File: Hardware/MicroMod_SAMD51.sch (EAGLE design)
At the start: 30 parts, among them J2 MICROMOD-2222, U1 W25QXX128MBIT-6X5-NO_CENTER, U2 ATSAMD51J20A-A, Y1 32.768kHz

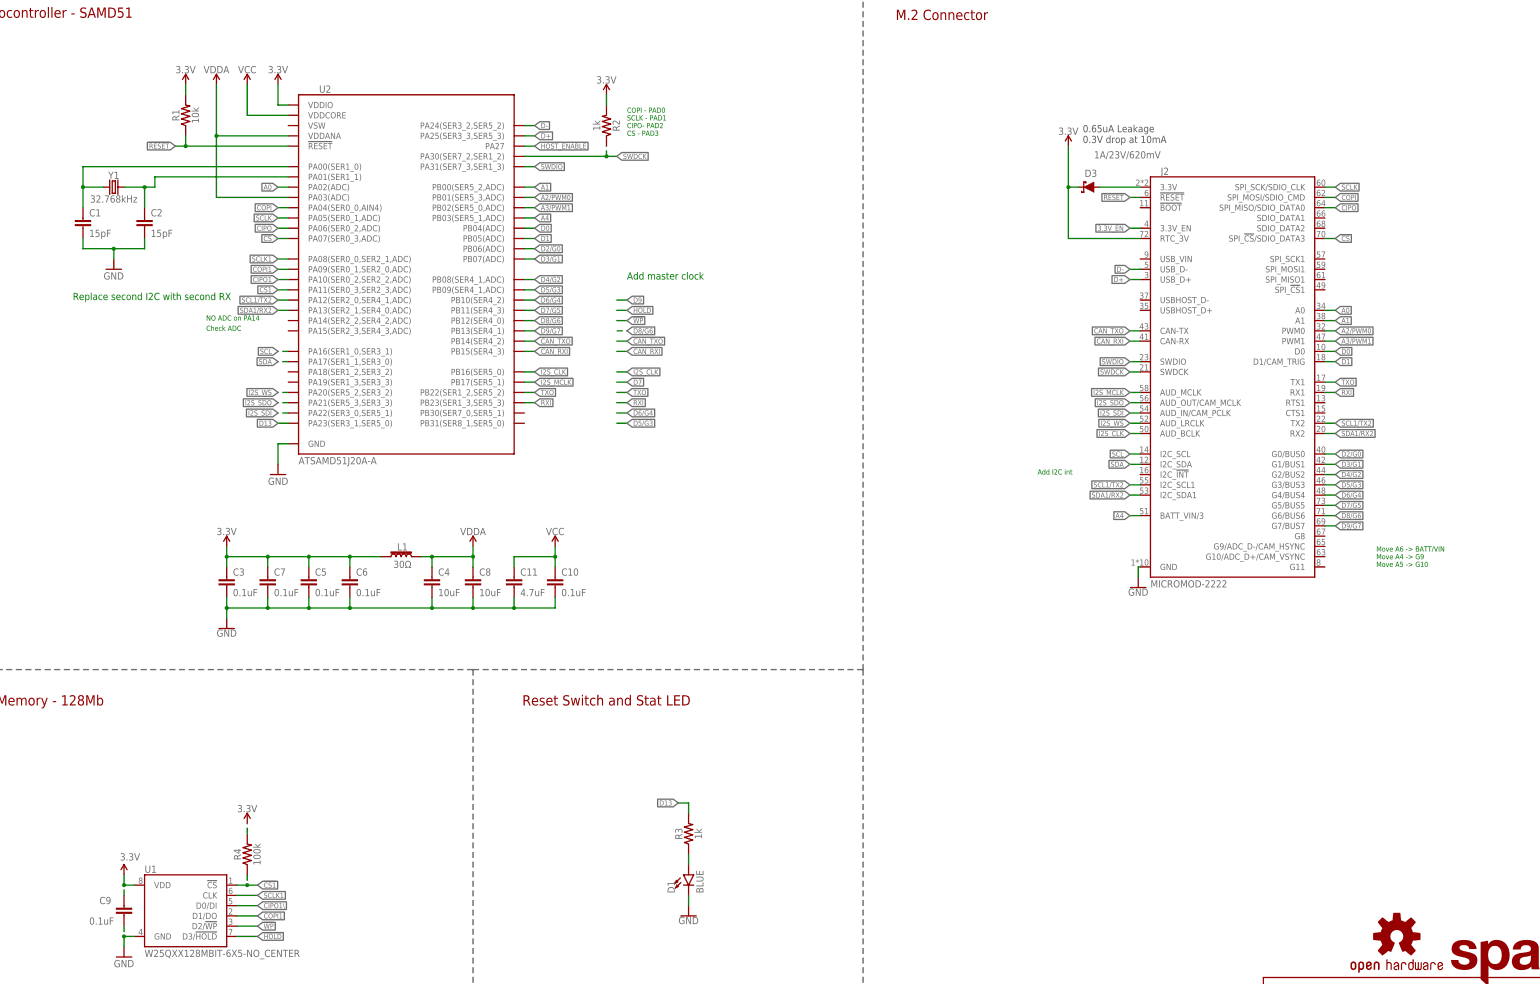
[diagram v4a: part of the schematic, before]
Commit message: Begins routing, removes old
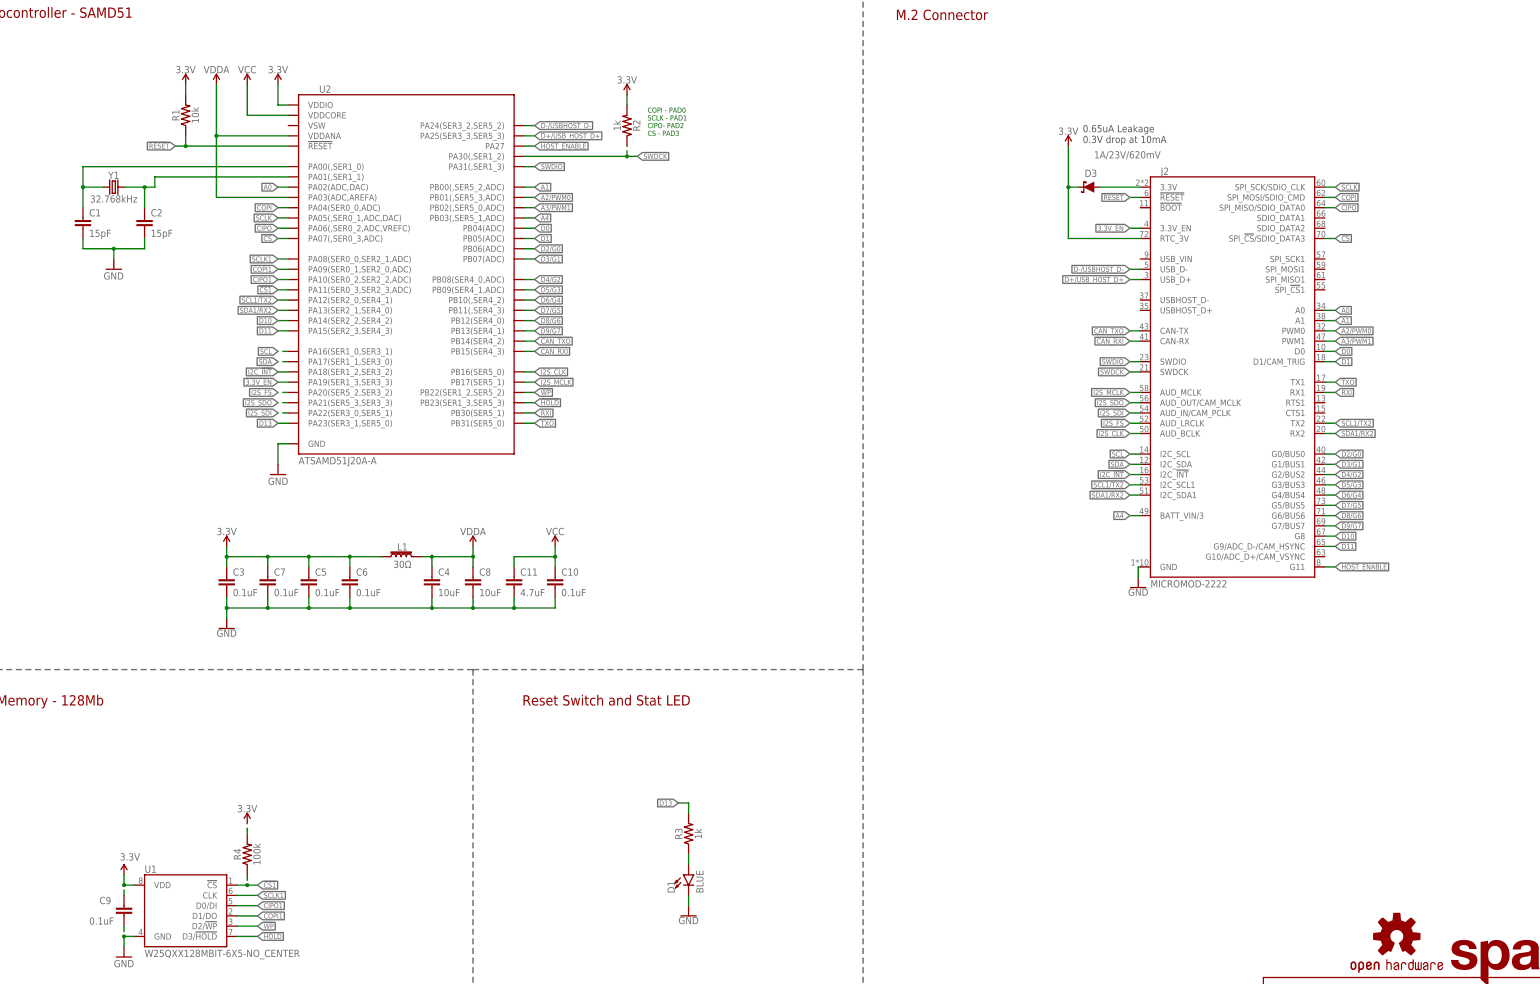
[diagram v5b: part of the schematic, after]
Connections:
- net D+ renamed D+/USB_HOST_D+
- net D- renamed D-/USBHOST_D-
- net I2S_WS renamed I2S_FS
- removed net CIPO1\: U1.D0/DI
- removed net CS1: U2.PA11(SER0_3,SER2_3,ADC)
- new net D10: J2.G8, U2.PA14(SER2_2,SER4_2)
- new net D11: J2.G9/ADC_D-/CAM_HSYNC, U2.PA15(SER2_3,SER4_3)
- new net I2C_!INT!: J2.I2C_!INT!, U2.PA18(SER1_2,SER3_2)
- net !CS: now also U2.PA07(,SER0_3,ADC); no longer U2.PA07(SER0_3,ADC)
- net !CS1!: now also U2.PA11(SER0_3,SER2_3,ADC)
- net !HOLD!: now also U2.PB23(SER1_3,SER5_3)
- net !WP!: now also U2.PB22(SER1_2,SER5_2)
- net 3.3V_EN: now also U2.PA19(SER1_3,SER3_3)
- net A0: now also U2.PA02(ADC,DAC); no longer U2.PA02(ADC)
- net A1: now also U2.PB00(,SER5_2,ADC); no longer U2.PB00(SER5_2,ADC)
- net A2/PWM0: now also U2.PB01(,SER5_3,ADC); no longer U2.PB01(SER5_3,ADC)
- net A3/PWM1: now also U2.PB02(,SER5_0,ADC); no longer U2.PB02(SER5_0,ADC)
- net A4: now also U2.PB03(,SER5_1,ADC); no longer U2.PB03(SER5_1,ADC)
- net CIPO: now also U2.PA06(,SER0_2,ADC,VREFC); no longer U2.PA06(SER0_2,ADC)
- net CIPO1: now also U1.D0/DI
- net COPI: now also U2.PA04(SER0_0,ADC); no longer U2.PA04(SER0_0,AIN4)
- net D4/G2: now also U2.PB08(SER4_0,ADC); no longer U2.PB08(SER4_1,ADC)
- net D6/G4: now also U2.PB10(,SER4_2); no longer U2.PB10(SER4_2)
- net D7/G5: now also U2.PB11(,SER4_3); no longer U2.PB11(SER4_3)
- net HOST_ENABLE: now also J2.G11
- net RXI: now also U2.PB30(SER5_1); no longer U2.PB23(SER1_3,SER5_3)
- net SCL1/TX2: now also U2.PA12(SER2_0,SER4_1); no longer U2.PA12(SER2_0,SER4_1,ADC)
- net SCLK: now also U2.PA05(,SER0_1,ADC,DAC); no longer U2.PA05(SER0_1,ADC)
- net SDA1/RX2: now also U2.PA13(SER2_1,SER4_0); no longer U2.PA13(SER2_1,SER4_0,ADC)
- net SWDCK: now also U2.PA30(,SER1_2); no longer U2.PA30(SER7_2,SER1_2)
- net SWDIO: now also U2.PA31(,SER1_3); no longer U2.PA31(SER7_3,SER1_3)
- net TXO: now also U2.PB31(SER5_0); no longer U2.PB22(SER1_2,SER5_2)
- net VDDA: now also U2.PA03(ADC,AREFA); no longer U2.PA03(ADC)
- net XIN32: now also U2.PA00(,SER1_0); no longer U2.PA00(SER1_0)
- net XOUT32: now also U2.PA01(,SER1_1); no longer U2.PA01(SER1_1)
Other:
- note removed: "Add I2C int"
- note removed: "Add master clock"
- note removed: "Check ADC"
- note removed: "Move A6 -> BATT/VIN Move A4 -> G9 Move A5 -> G10"
- note removed: "NO ADC on PA14"
- note removed: "Replace second I2C with second RX"
- moved on the sheet: R2

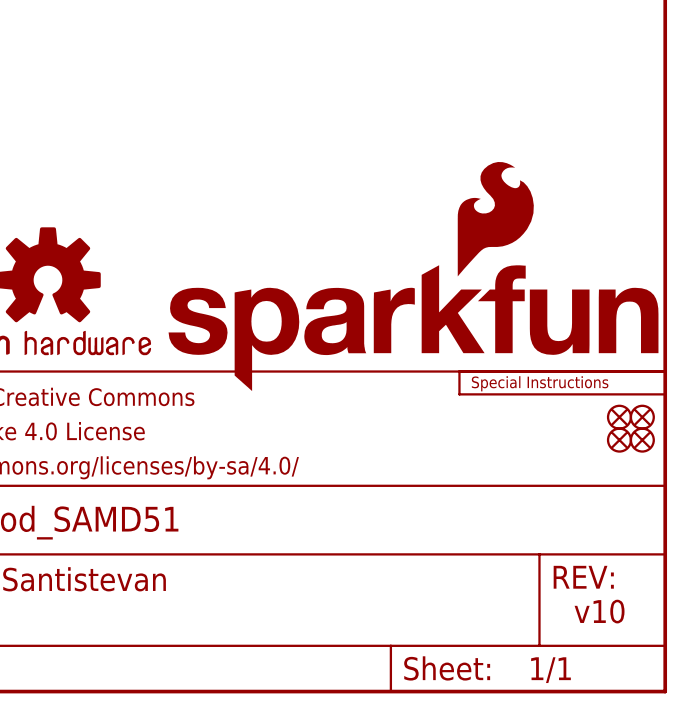
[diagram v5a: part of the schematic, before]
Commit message: Updates SparkFun silk, rolls version to v11, fixes some traces that were not crossing others at 90 degrees.
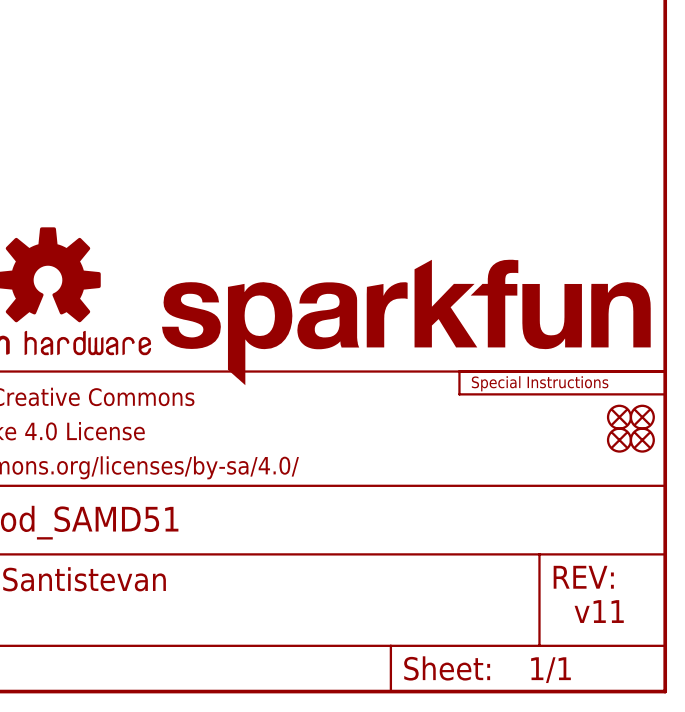
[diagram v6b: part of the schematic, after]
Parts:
- LOGO6: value SFE_LOGO_NAME_FLAME.1_INCH -> SFE_LOGO_NAME.1_INCH; device SparkFun-Aesthetics:SFE_LOGO_NAME_FLAME.1_INCH -> SparkFun-Aesthetics:SFE_LOGO_NAME.1_INCH
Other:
- note added: "v11"
- note removed: "v10"
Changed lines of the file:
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@@
 <part name="LOGO2" library="SparkFun-Aesthetics" deviceset="OSHW-LOGO" device="MINI" value="OSHW-LOGOMINI"/>
 <part name="LOGO5" library="SparkFun-Aesthetics" deviceset="SPECIAL_INSTRUCTIONS" device="-ORDERING"/>
-<part name="LOGO6" library="SparkFun-Aesthetics" deviceset="SFE_LOGO_NAME_FLAME" device=".1_INCH"/>
+<part name="LOGO6" library="SparkFun-Aesthetics" deviceset="SFE_LOGO_NAME" device=".1_INCH"/>
 <part name="FRAME2" library="SparkFun-Aesthetics" deviceset="FRAME-LEDGER" device=""/>
 <part name="D1" library="SparkFun-LED" deviceset="LED-BLUE" device="0603" value="BLUE"/>
@@
 <sheet>
 <plain>
-<text x="421.64" y="7.62" size="2.54" layer="94" font="vector">v10</text>
+<text x="421.64" y="7.62" size="2.54" layer="94" font="vector">v11</text>
 <text x="250.64" y="273.78" size="2.54" layer="94" font="vector" align="center">M.2 Connector</text>
 <wire x1="231.14" y1="279.4" x2="231.14" y2="111.76" width="0.1524" layer="97" style="longdash"/>
@@
 <instance part="LOGO2" gate="G$1" x="363.22" y="45.72" smashed="yes"/>
 <instance part="LOGO5" gate="G$1" x="408.94" y="33.02" smashed="yes"/>
-<instance part="LOGO6" gate="G$1" x="375.92" y="33.02" smashed="yes"/>
+<instance part="LOGO6" gate="G$1" x="373.888" y="34.036" smashed="yes"/>
 <instance part="FRAME2" gate="G$1" x="0" y="0" smashed="yes"/>
 <instance part="FRAME2" gate="G$2" x="330.2" y="0" smashed="yes">

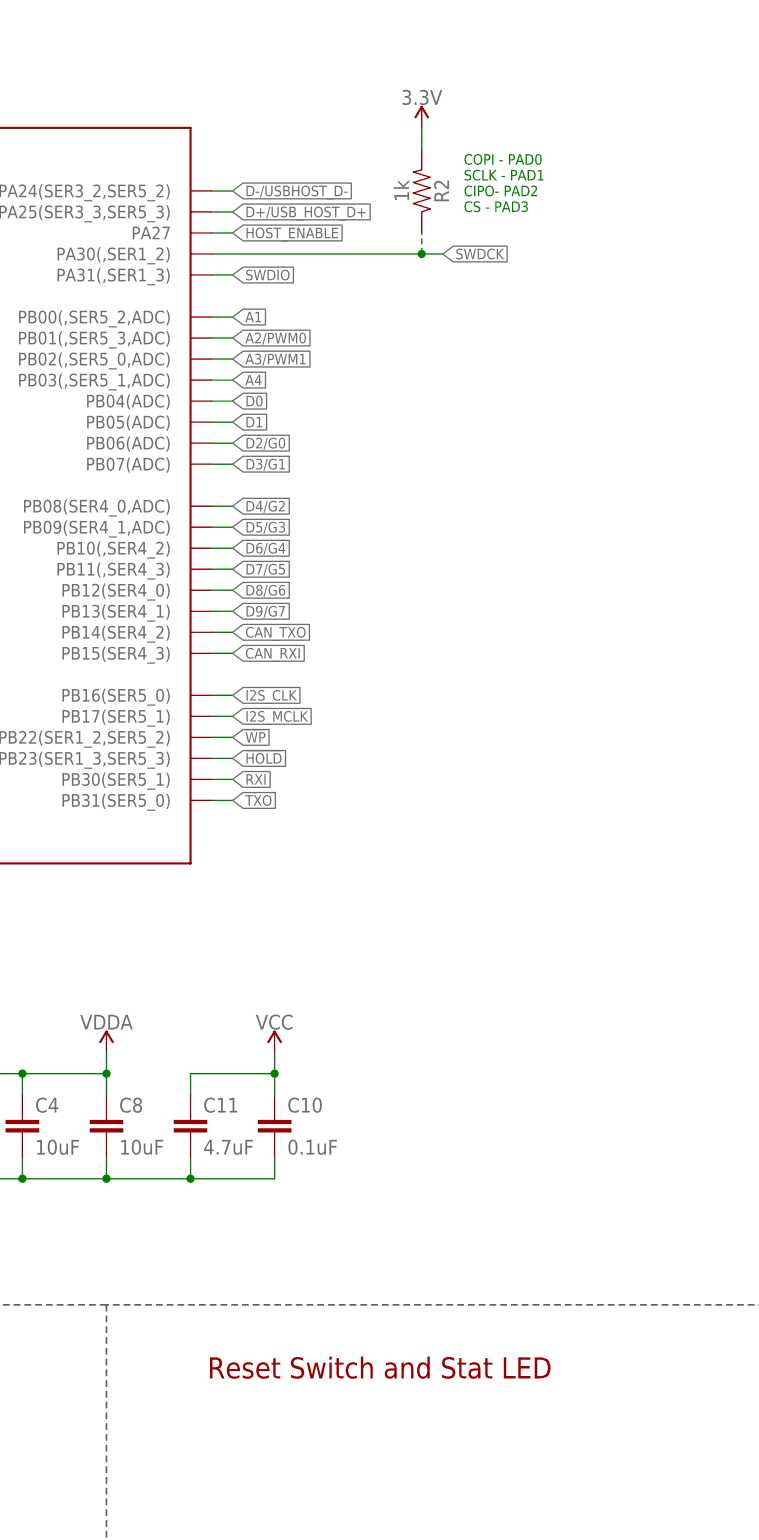
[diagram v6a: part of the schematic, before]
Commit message: Moves cap at top of board, adjusts USB differential pair
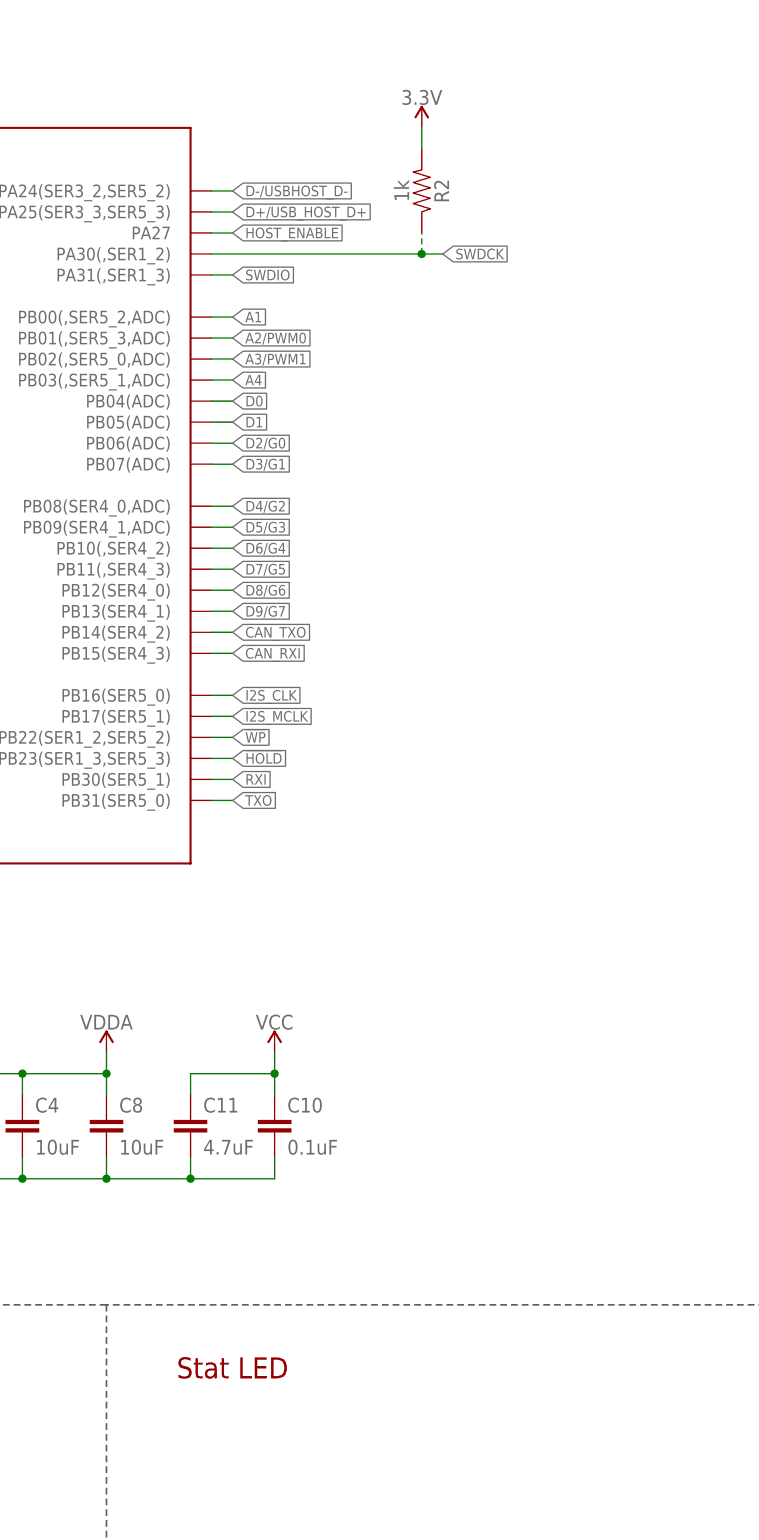
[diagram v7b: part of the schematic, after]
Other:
- note added: "Stat LED"
- note removed: "COPI - PAD0 SCLK - PAD1 CIPO- PAD2 CS - PAD3"
- note removed: "Reset Switch and Stat LED"
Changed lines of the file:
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@@
 <clearance class="1" value="0.2032"/>
+</class>
+<class number="2" name="USB" width="0.1016" drill="0">
+<clearance class="2" value="0.0762"/>
 </class>
 </classes>
@@
 <text x="30.48" y="274.32" size="2.54" layer="94" font="vector" align="center">Microcontroller - SAMD51</text>
 <text x="25.4" y="104.14" size="2.54" layer="94" font="vector" align="center">Flash Memory - 128Mb</text>
-<text x="167.64" y="104.14" size="2.54" layer="94" font="vector" align="center">Reset Switch and Stat LED</text>
+<text x="149.86" y="104.14" size="2.54" layer="94" font="vector" align="center">Stat LED</text>
 <wire x1="231.14" y1="111.76" x2="231.14" y2="0" width="0.2032" layer="97" style="longdash"/>
 <text x="349.758" y="11.176" size="2.54" layer="94" font="vector">Elias Santistevan</text>
 <text x="285.496" y="242.062" size="1.778" layer="97">0.65uA Leakage
 0.3V drop at 10mA</text>
-<text x="177.8" y="243.84" size="1.27" layer="91">COPI - PAD0
-SCLK - PAD1
-CIPO- PAD2
-CS - PAD3</text>
 </plain>
 <instances>
@@
 </segment>
 </net>
-<net name="D-/USBHOST_D-" class="0">
+<net name="D-/USBHOST_D-" class="2">
 <segment>
 <pinref part="J2" gate="J1" pin="USB_D-"/>
@@
 </segment>
 </net>
-<net name="D+/USB_HOST_D+" class="0">
+<net name="D+/USB_HOST_D+" class="2">
 <segment>
 <pinref part="J2" gate="J1" pin="USB_D+"/>

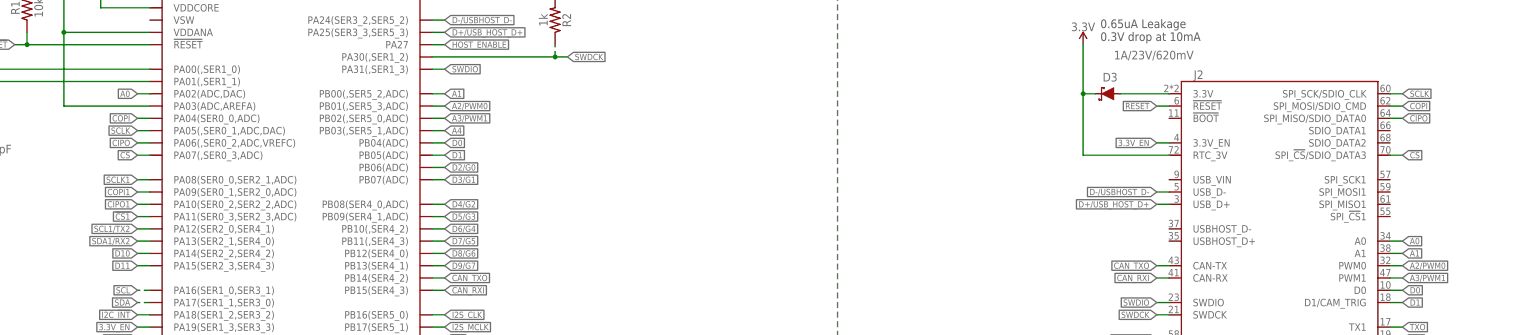
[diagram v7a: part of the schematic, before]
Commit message: Increases dimension line width, fixes some proportional text, relabels A0 to includ DAC
* Adds dimension measurements to measures layer
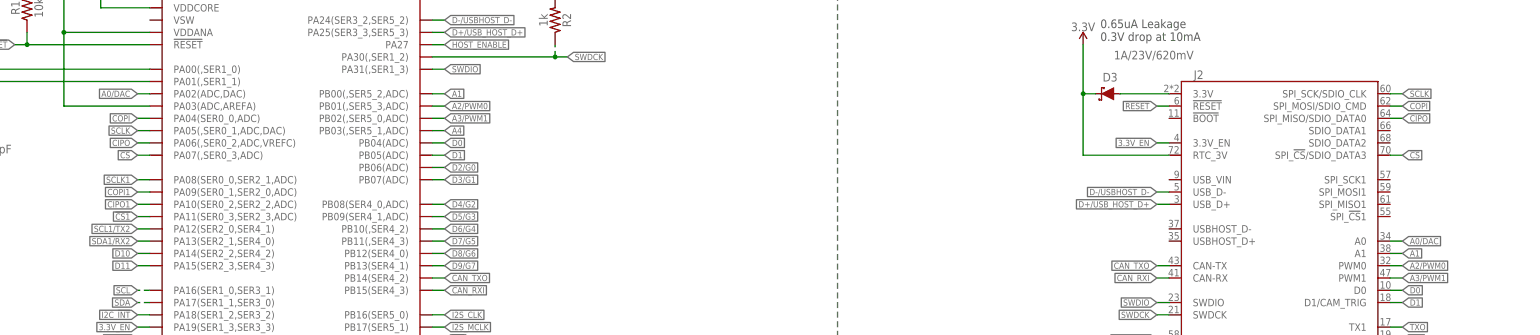
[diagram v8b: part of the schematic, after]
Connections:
- net A0 renamed A0/DAC
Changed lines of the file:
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@@
 <wire x1="231.14" y1="111.76" x2="231.14" y2="0" width="0.2032" layer="97" style="longdash"/>
 <text x="349.758" y="11.176" size="2.54" layer="94" font="vector">Elias Santistevan</text>
-<text x="285.496" y="242.062" size="1.778" layer="97">0.65uA Leakage
+<text x="285.496" y="242.062" size="1.778" layer="97" font="vector">0.65uA Leakage
 0.3V drop at 10mA</text>
 </plain>
@@
 </segment>
 </net>
-<net name="A0" class="0">
+<net name="A0/DAC" class="0">
 <segment>
 <wire x1="88.9" y1="231.14" x2="86.36" y2="231.14" width="0.1524" layer="91"/>
